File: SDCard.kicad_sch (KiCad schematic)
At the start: 5 parts, among them J7 Micro_SD_Card_Det, U22 RT9742GGJ5

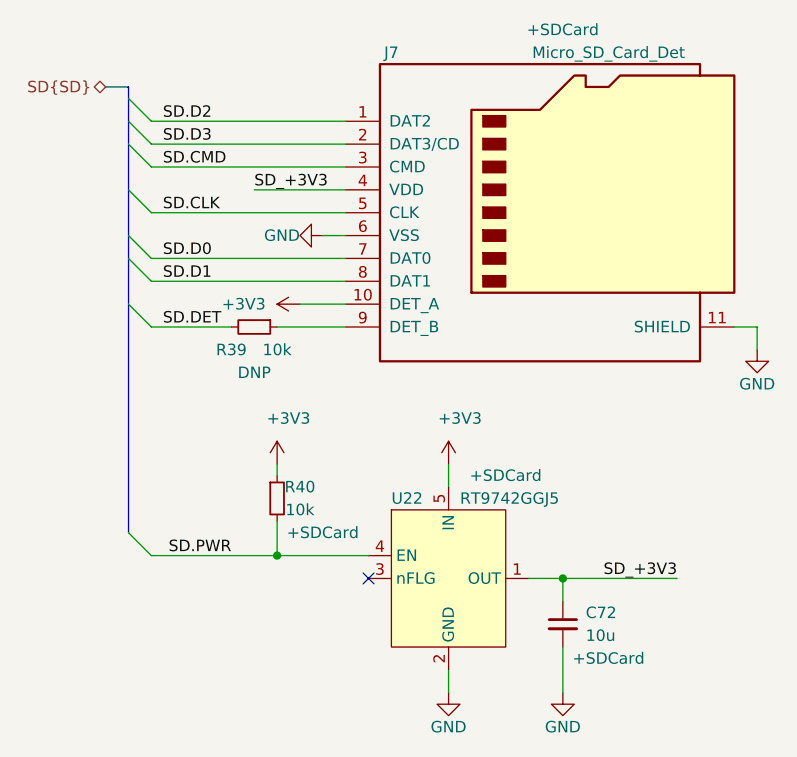
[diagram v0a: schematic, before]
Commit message: Yellow Proto1
Changes:
-name changed to yellow
-moved to 24-pin CP2102N
-routing

Signed-off-by: Dominik Sliwa <dominik@sliwa.io>
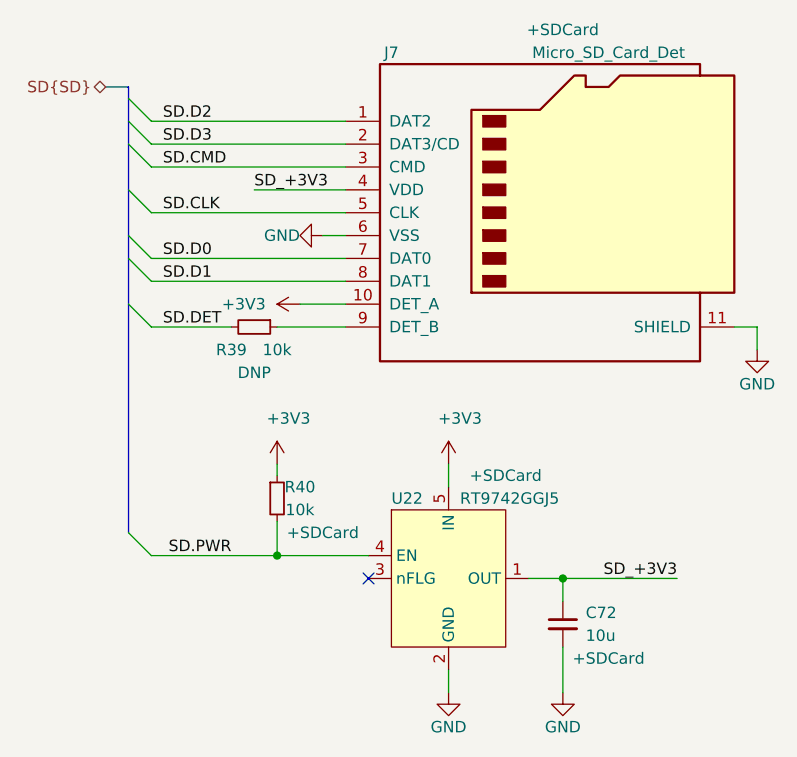
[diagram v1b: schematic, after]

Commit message: Rename Amber to Yellow everywhere
Signed-off-by: Stefan Agner <stefan@agner.ch>
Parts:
- U22: symbol Amber:RT9742GGJ5 -> Yellow:RT9742GGJ5
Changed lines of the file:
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@@
     (pin "9")
   )
-  (symbol (lib_id "Amber:RT9742GGJ5") (at 91.44 111.76 0) (unit 1)
+  (symbol (lib_id "Yellow:RT9742GGJ5") (at 91.44 111.76 0) (unit 1)
     (in_bom yes) (on_board yes)
     (property "Reference" "U22" (id 0) (at 85.09 102.87 0)
